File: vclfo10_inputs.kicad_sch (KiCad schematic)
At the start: 91 parts, among them Q2 BC547, U5 LM358, U6 LM358, U7 LM358, U8 LM358

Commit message: Routing done
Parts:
- J_LFO_RANGE1, J_SYNC_MODE1: footprint Connector_PinSocket_2.54mm:PinSocket_1x05_P2.54mm_Horizontal -> My Stuff:PinSocket_1x05_P2.54mm_Horizontal_no_silkscreen
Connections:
- net GND: now also RV_LFO_RANGE1.1, RV_LFO_RANGE1.MP (MountPin), RV_SYNC_MODE1.1, RV_SYNC_MODE1.MP (MountPin)
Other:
- moved on the sheet: RV_SYNC_MODE1

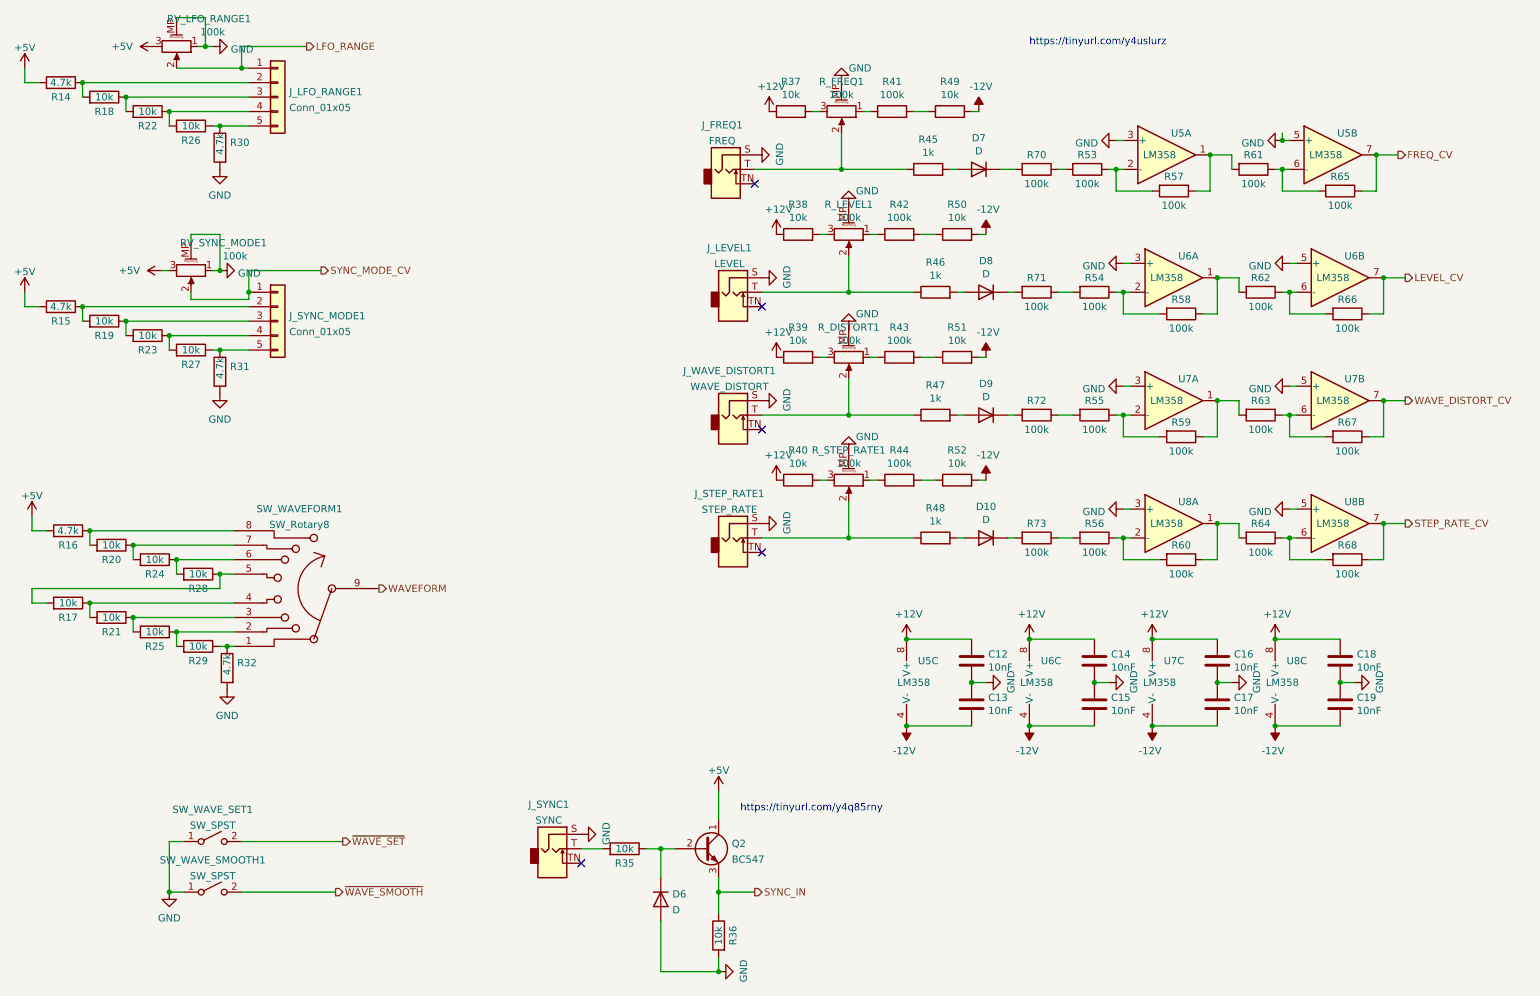
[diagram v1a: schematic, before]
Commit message: Geographic reannotate and silkscreen cleanup
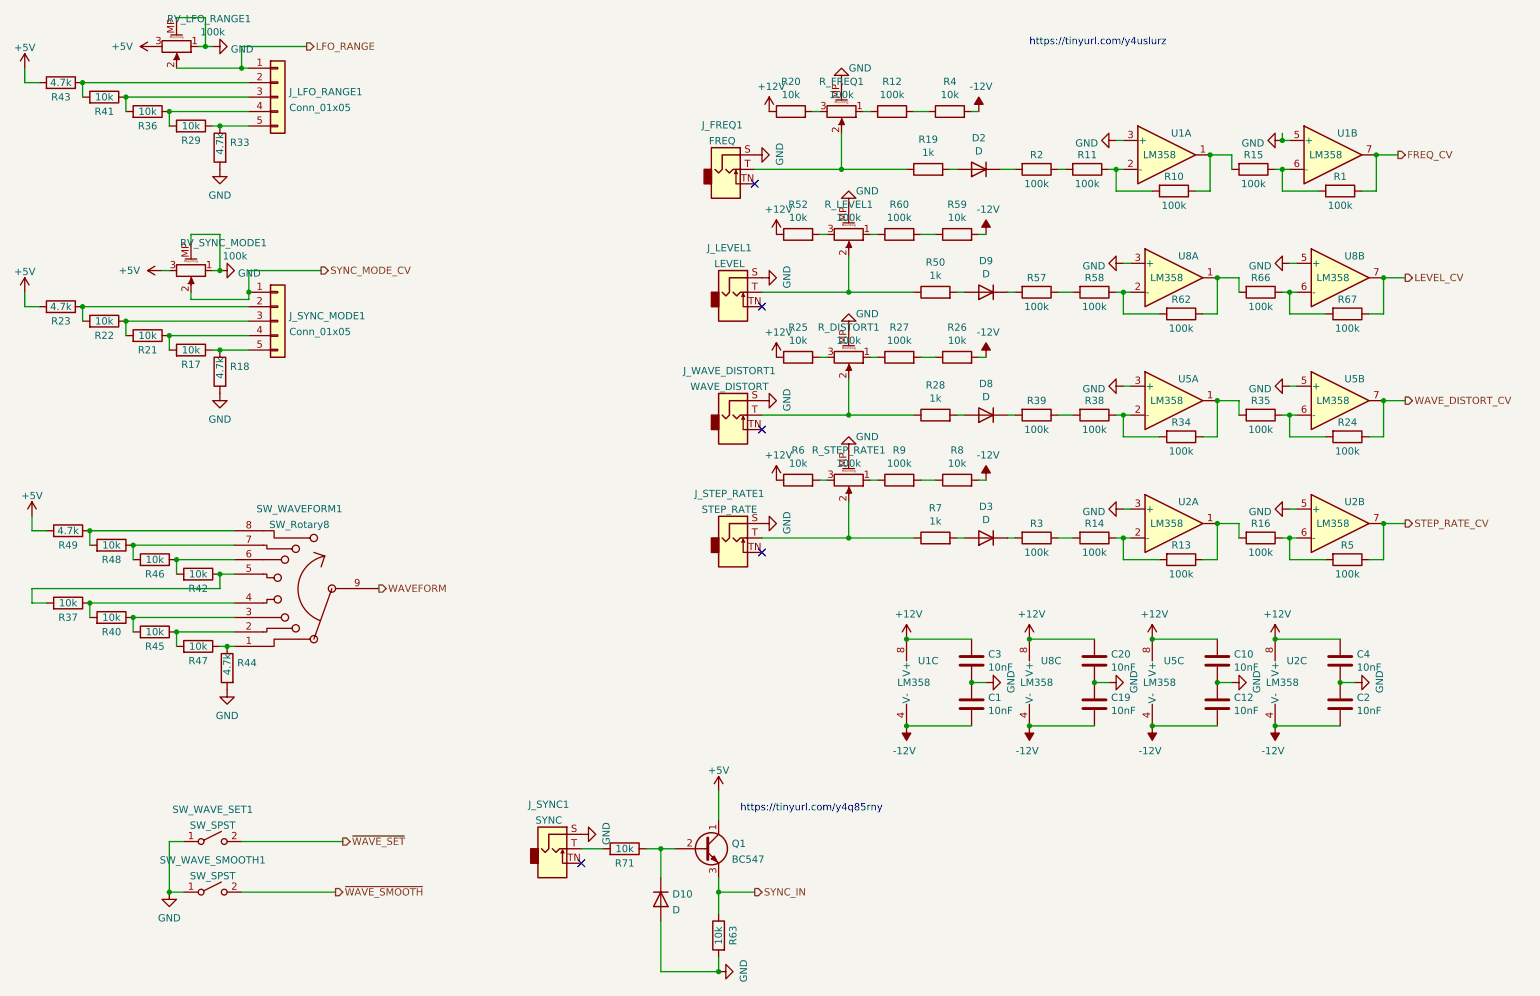
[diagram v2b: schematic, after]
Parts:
- renumbered C13 to C1, C16 to C10, C17 to C12, C15 to C19, C19 to C2, C14 to C20, C12 to C3, C18 to C4, D6 to D10, D7 to D2, D10 to D3, D9 to D8, D8 to D9, Q2 to Q1, R65 to R1, R57 to R10, R53 to R11, R41 to R12, R60 to R13, R56 to R14, R61 to R15, R64 to R16, R27 to R17, R31 to R18, R45 to R19, R70 to R2, R37 to R20, R23 to R21, R19 to R22, R15 to R23, R67 to R24, R39 to R25, R51 to R26, R43 to R27, R47 to R28, R26 to R29, R73 to R3, R30 to R33, R59 to R34, R63 to R35, R22 to R36, R17 to R37, R55 to R38, R72 to R39, R49 to R4, R21 to R40, R18 to R41, R28 to R42, R14 to R43, R32 to R44, R25 to R45, R24 to R46, R29 to R47, R20 to R48, R16 to R49, R68 to R5, R46 to R50, R38 to R52, R71 to R57, R54 to R58, R50 to R59, R40 to R6, R42 to R60, R58 to R62, R36 to R63, R62 to R66, R66 to R67, R48 to R7, R35 to R71, R52 to R8, R44 to R9, U5 to U1, U8 to U2, U7 to U5, U6 to U8

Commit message: Update title block on schematic and pcb sheets
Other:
- title: ED VCLFO -> VCLFO10
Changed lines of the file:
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@@
   (paper "A4")
   (title_block
-    (title "ED VCLFO")
-    (date "2022-05-15")
+    (title "VCLFO10")
+    (date "2022-06-29")
     (rev "1.0")
     (company "RobotDialogs")
